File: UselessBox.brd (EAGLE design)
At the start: 49.5 x 39.4 mm, 20 parts, among them Q2 MJE182-VERTICAL, U2 5V, X1 SCREW-TERM-3, X2 SCREW-TERM-3

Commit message: Better power traces and polish tweaks
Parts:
- moved Q2 14.0 mm to (45.7, 50.2)
- moved C6 7.62 mm to (45.1, 38.1)
- moved R2 7.62 mm to (45.7, 45.7)
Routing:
- net N$12: track 23.2 -> 30.8 mm
- net VIN: track 53.1 -> 60.6 mm
- net N$13: track 30.4 -> 25.4 mm
- net N$8: track 24.4 -> 25.1 mm
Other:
- board text added: "SIG"
- board text removed: "CTRL"

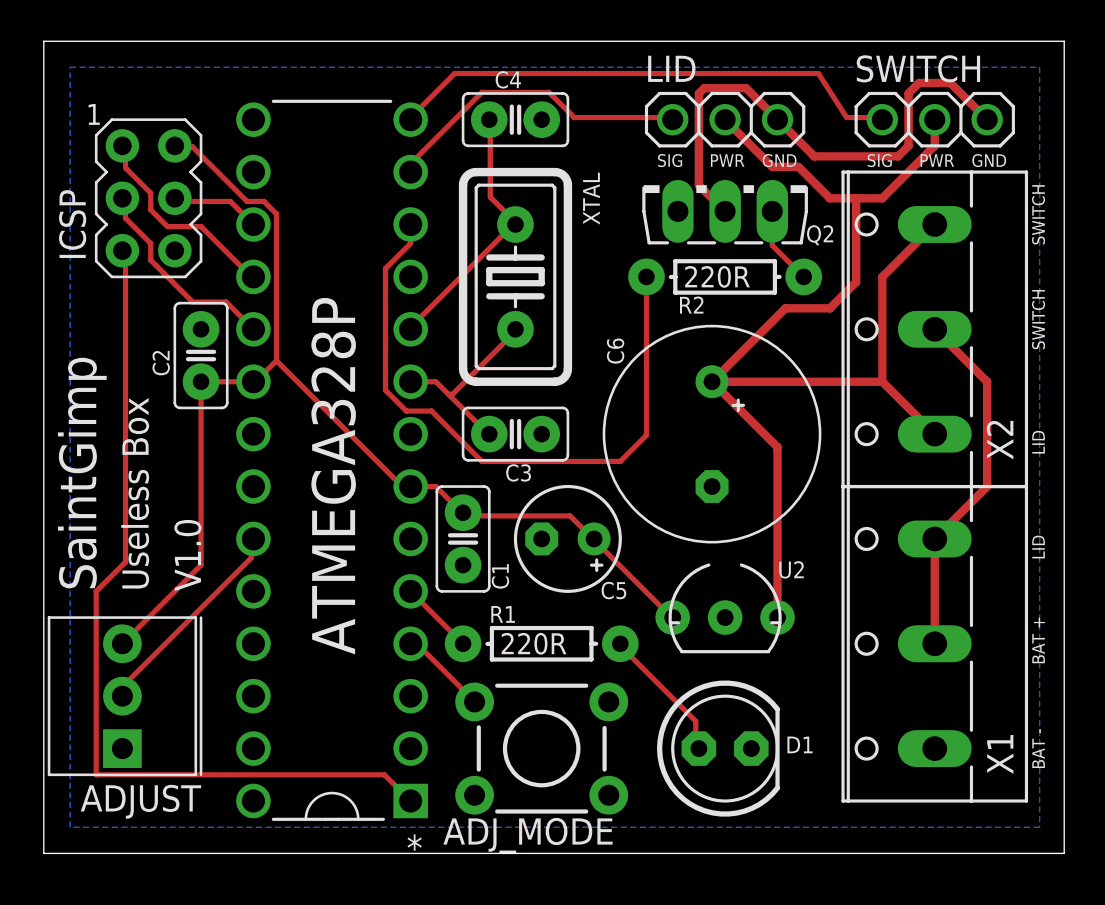
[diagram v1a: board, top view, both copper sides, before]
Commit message: Update size of bypass caps
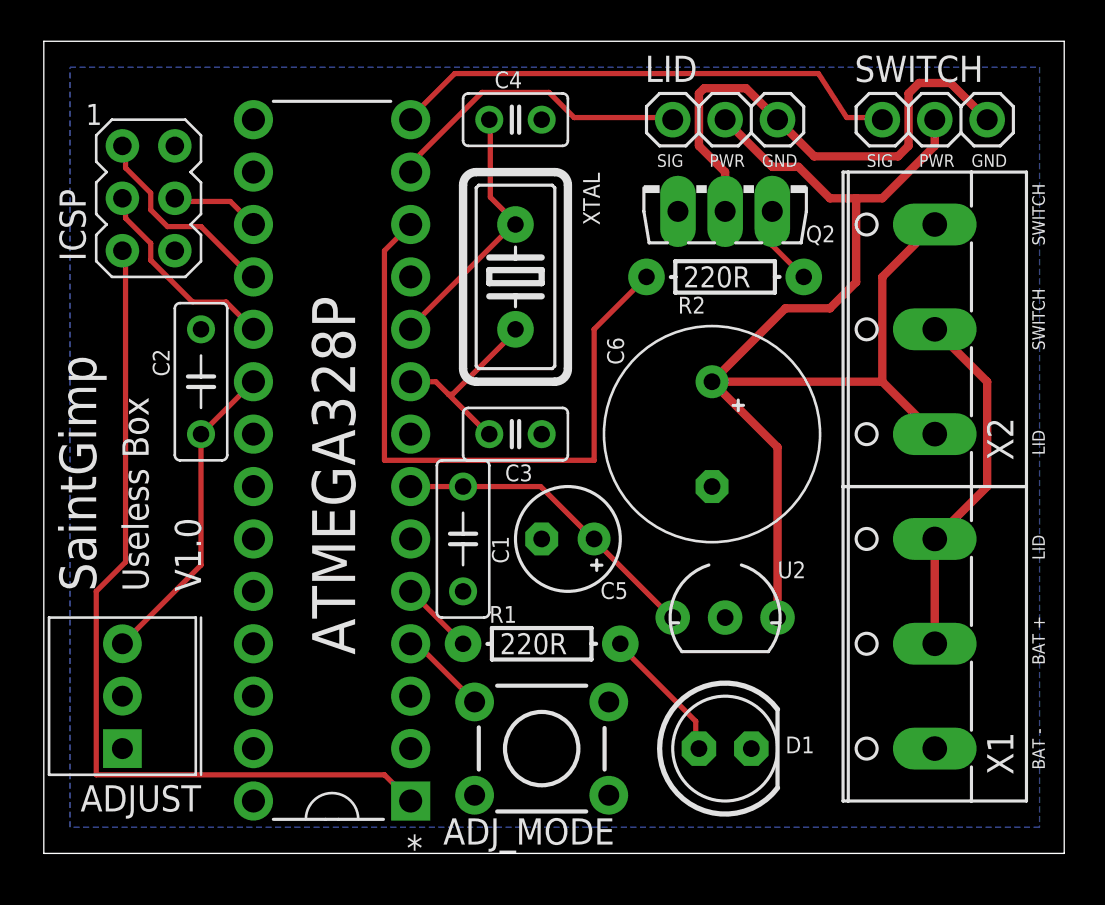
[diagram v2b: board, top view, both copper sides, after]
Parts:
- C1, C2: device SaintGimp:CAPACITOR-2.5MM -> SaintGimp:CAPACITOR-5MM
- moved C1 1.27 mm to (33.0, 33.0)
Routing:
- net VCC: track 56.1 -> 30.7 mm
- net N$15: track 10.3 -> 0.76 mm
- net N$12: track 30.8 -> 32.1 mm
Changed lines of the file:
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@@
 <layer number="97" name="Info" color="7" fill="1" visible="no" active="no"/>
 <layer number="98" name="Guide" color="6" fill="1" visible="no" active="no"/>
+<layer number="99" name="SpiceOrder" color="7" fill="1" visible="no" active="no"/>
 <layer number="100" name="Muster" color="7" fill="1" visible="no" active="no"/>
 <layer number="101" name="Patch_Top" color="12" fill="4" visible="yes" active="yes"/>
@@
 <layer number="111" name="LPC17xx" color="7" fill="1" visible="yes" active="yes"/>
 <layer number="112" name="tSilk" color="7" fill="1" visible="yes" active="yes"/>
+<layer number="113" name="IDFDebug" color="7" fill="1" visible="yes" active="yes"/>
 <layer number="116" name="Patch_BOT" color="9" fill="4" visible="yes" active="yes"/>
 <layer number="121" name="_tsilk" color="7" fill="1" visible="yes" active="yes"/>
@@
 <layer number="251" name="SMDround" color="7" fill="1" visible="no" active="no"/>
 <layer number="254" name="cooling" color="7" fill="1" visible="yes" active="yes"/>
+<layer number="255" name="routoute" color="7" fill="1" visible="yes" active="yes"/>
 </layers>
 <board>
@@
 <param name="msMicroVia" value="13mil"/>
 <param name="msBlindViaRatio" value="0.5"/>
-<param name="rvPadTop" value="0.25"/>
+<param name="rvPadTop" value="0.35"/>
 <param name="rvPadInner" value="0.25"/>
-<param name="rvPadBottom" value="0.25"/>
+<param name="rvPadBottom" value="0.35"/>
 <param name="rvViaOuter" value="0.25"/>
 <param name="rvViaInner" value="0.25"/>
@@
 <attribute name="VALUE" x="30.1244" y="17.145" size="2.0828" layer="27" ratio="10" rot="SR180"/>
 </element>
-<element name="C1" library="SaintGimp" package="CAPACITOR-2.5MM" value="1uF" x="33.02" y="31.75" smashed="yes" rot="R90">
-<attribute name="NAME" x="35.2374375" y="30.5553125" size="0.8128" layer="25" rot="R90"/>
-<attribute name="VALUE" x="35.56" y="31.242" size="1.016" layer="27" rot="R90"/>
-</element>
-<element name="C2" library="SaintGimp" package="CAPACITOR-2.5MM" value="1uF" x="20.32" y="40.64" smashed="yes" rot="R90">
+<element name="C1" library="SaintGimp" package="CAPACITOR-5MM" value="1uF" x="33.02" y="33.02" smashed="yes" rot="R90">
+<attribute name="NAME" x="35.2374375" y="31.8253125" size="0.8128" layer="25" rot="R90"/>
+<attribute name="VALUE" x="35.56" y="32.512" size="1.016" layer="27" rot="R90"/>
+</element>
+<element name="C2" library="SaintGimp" package="CAPACITOR-5MM" value="1uF" x="20.32" y="40.64" smashed="yes" rot="R90">
 <attribute name="NAME" x="18.796" y="40.894" size="0.8128" layer="25" rot="R90"/>
 <attribute name="VALUE" x="22.86" y="40.132" size="1.016" layer="27" rot="R90"/>
@@
 <contactref element="C5" pad="+"/>
 <contactref element="ADJUST" pad="P$3"/>
-<wire x1="31.6992" y1="35.56" x2="30.48" y2="35.56" width="0.254" layer="1"/>
-<wire x1="32.9184" y1="34.3408" x2="31.6992" y2="35.56" width="0.254" layer="1"/>
-<wire x1="32.9184" y1="34.3408" x2="33.02" y2="34.29" width="0.254" layer="1"/>
 <wire x1="43.0784" y1="29.2608" x2="39.4208" y2="32.9184" width="0.254" layer="1"/>
 <wire x1="39.4208" y1="32.9184" x2="39.37" y2="33.02" width="0.254" layer="1"/>
 <wire x1="43.0784" y1="29.2608" x2="43.18" y2="29.21" width="0.254" layer="1"/>
-<wire x1="38.2016" y1="34.1376" x2="33.1216" y2="34.1376" width="0.254" layer="1"/>
-<wire x1="39.2176" y1="33.1216" x2="38.2016" y2="34.1376" width="0.254" layer="1"/>
-<wire x1="33.1216" y1="34.1376" x2="33.02" y2="34.29" width="0.254" layer="1"/>
 <wire x1="39.2176" y1="33.1216" x2="39.37" y2="33.02" width="0.254" layer="1"/>
-<wire x1="19.9136" y1="52.0192" x2="19.1008" y2="52.0192" width="0.254" layer="1"/>
-<wire x1="22.5552" y1="49.3776" x2="19.9136" y2="52.0192" width="0.254" layer="1"/>
-<wire x1="23.368" y1="49.3776" x2="22.5552" y2="49.3776" width="0.254" layer="1"/>
-<wire x1="23.9776" y1="48.768" x2="23.368" y2="49.3776" width="0.254" layer="1"/>
-<wire x1="23.9776" y1="41.656" x2="23.9776" y2="48.768" width="0.254" layer="1"/>
-<wire x1="22.9616" y1="40.64" x2="23.9776" y2="41.656" width="0.254" layer="1"/>
-<wire x1="19.1008" y1="52.0192" x2="19.05" y2="52.07" width="0.254" layer="1"/>
-<wire x1="22.9616" y1="40.64" x2="22.86" y2="40.64" width="0.254" layer="1"/>
-<wire x1="22.86" y1="40.64" x2="20.32" y2="40.64" width="0.254" layer="1"/>
-<wire x1="30.0736" y1="35.56" x2="30.48" y2="35.56" width="0.254" layer="1"/>
-<wire x1="23.9776" y1="41.656" x2="30.0736" y2="35.56" width="0.254" layer="1"/>
-<wire x1="20.32" y1="40.64" x2="20.32" y2="31.75" width="0.254" layer="1"/>
+<wire x1="22.86" y1="40.64" x2="20.32" y2="38.1" width="0.254" layer="1"/>
+<wire x1="20.32" y1="38.1" x2="20.32" y2="31.75" width="0.254" layer="1"/>
 <wire x1="20.32" y1="31.75" x2="16.51" y2="27.94" width="0.254" layer="1"/>
+<wire x1="30.48" y1="35.56" x2="33.02" y2="35.56" width="0.254" layer="1"/>
+<wire x1="33.02" y1="35.56" x2="36.7792" y2="35.56" width="0.254" layer="1"/>
+<wire x1="36.7792" y1="35.56" x2="39.2176" y2="33.1216" width="0.254" layer="1"/>
+<wire x1="22.86" y1="40.64" x2="19.05" y2="52.07" width="0" layer="19" extent="1-1"/>
+<wire x1="30.48" y1="35.56" x2="22.86" y2="40.64" width="0" layer="19" extent="1-1"/>
 </signal>
 <signal name="N$6">
@@
 <contactref element="ATMEGA328P" pad="12"/>
 <contactref element="R2" pad="P$1"/>
-<wire x1="30.48" y1="47.3456" x2="30.48" y2="48.26" width="0.254" layer="1"/>
-<wire x1="29.2608" y1="46.1264" x2="30.48" y2="47.3456" width="0.254" layer="1"/>
-<wire x1="29.2608" y1="40.2336" x2="29.2608" y2="46.1264" width="0.254" layer="1"/>
-<wire x1="30.2768" y1="39.2176" x2="29.2608" y2="40.2336" width="0.254" layer="1"/>
-<wire x1="31.496" y1="39.2176" x2="30.2768" y2="39.2176" width="0.254" layer="1"/>
-<wire x1="33.9344" y1="36.7792" x2="31.496" y2="39.2176" width="0.254" layer="1"/>
-<wire x1="40.64" y1="36.7792" x2="33.9344" y2="36.7792" width="0.254" layer="1"/>
-<wire x1="40.64" y1="36.7792" x2="41.91" y2="38.0492" width="0.254" layer="1"/>
-<wire x1="41.91" y1="38.0492" x2="41.91" y2="45.72" width="0.254" layer="1"/>
+<wire x1="30.48" y1="48.26" x2="29.21" y2="46.99" width="0.254" layer="1"/>
+<wire x1="29.21" y1="46.99" x2="29.21" y2="36.83" width="0.254" layer="1"/>
+<wire x1="29.21" y1="36.83" x2="39.37" y2="36.83" width="0.254" layer="1"/>
+<wire x1="39.37" y1="36.83" x2="39.37" y2="43.18" width="0.254" layer="1"/>
+<wire x1="39.37" y1="43.18" x2="41.91" y2="45.72" width="0.254" layer="1"/>
 </signal>
 <signal name="N$13">
@@
 <wire x1="46.736" y1="54.864" x2="44.704" y2="54.864" width="0.4064" layer="1"/>
 <wire x1="44.704" y1="54.864" x2="44.45" y2="54.61" width="0.4064" layer="1"/>
-<wire x1="44.45" y1="54.61" x2="44.45" y2="50.165" width="0.4064" layer="1"/>
-<wire x1="44.45" y1="50.165" x2="45.72" y2="48.895" width="0.4064" layer="1"/>
+<wire x1="44.45" y1="54.61" x2="44.45" y2="52.07" width="0.4064" layer="1"/>
+<wire x1="44.45" y1="52.07" x2="45.72" y2="50.8" width="0.4064" layer="1"/>
+<wire x1="45.72" y1="50.8" x2="45.72" y2="48.895" width="0.4064" layer="1"/>
 </signal>
 <signal name="N$14">
@@
 <contactref element="ADJUST" pad="P$2"/>
 <contactref element="ATMEGA328P" pad="23"/>
-<wire x1="22.7584" y1="32.1056" x2="22.7584" y2="32.9184" width="0.254" layer="1"/>
-<wire x1="16.6624" y1="26.0096" x2="22.7584" y2="32.1056" width="0.254" layer="1"/>
 <wire x1="16.6624" y1="25.4" x2="16.6624" y2="26.0096" width="0.254" layer="1"/>
-<wire x1="22.7584" y1="32.9184" x2="22.86" y2="33.02" width="0.254" layer="1"/>
 <wire x1="16.6624" y1="25.4" x2="16.51" y2="25.4" width="0.254" layer="1"/>
+<wire x1="16.6624" y1="26.0096" x2="22.86" y2="33.02" width="0" layer="19" extent="1-1"/>
 </signal>
 <signal name="N$18">

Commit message: Update parts from library
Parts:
- ADJUST: device SaintGimp:3362U -> SaintGimp:POT-3362U
- ADJ_MODE: device SaintGimp:TACTILE-PTH -> SaintGimp:TACTILE-SWITCH-6MM
- ATMEGA328P: device SaintGimp:DIP254P762X457-28 -> SaintGimp:DIP28
- Q2: value MJE182-VERTICAL -> MJE182-V; device SaintGimp:TO126AV -> SaintGimp:TO225AA-V
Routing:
- net VCC: track 30.7 -> 57.6 mm
- net N$15: track 0.76 -> 9.92 mm
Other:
- board text added: "V1.1"
- board text removed: "V1.0"
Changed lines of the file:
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@@
 <text x="15.24" y="30.48" size="1.778" layer="121" rot="R90">SaintGimp</text>
 <text x="17.78" y="30.48" size="1.27" layer="121" rot="R90">Useless Box</text>
-<text x="20.32" y="30.48" size="1.27" layer="121" rot="R90">V1.0</text>
+<text x="20.32" y="30.48" size="1.27" layer="121" rot="R90">V1.1</text>
 <text x="47.498" y="51.054" size="0.6096" layer="121">GND</text>
 <text x="57.658" y="51.054" size="0.6096" layer="121">GND</text>
@@
 </class>
 </classes>
-<designrules name="OSHPark *">
+<designrules name="OSHPark">
 <description language="de">&lt;b&gt;EAGLE Design Rules&lt;/b&gt;
 &lt;p&gt;
@@
 </autorouter>
 <elements>
-<element name="ATMEGA328P" library="SaintGimp" package="DIP254P762X457-28" value="ATMEGA328P-PU" x="22.86" y="53.34" smashed="yes" rot="R180">
+<element name="ATMEGA328P" library="SaintGimp" package="DIP28" value="ATMEGA328P-PU" x="22.86" y="53.34" smashed="yes" rot="R180">
 <attribute name="PACKAGE" value="PDIP-28" x="22.86" y="53.34" size="1.778" layer="27" rot="R180" display="off"/>
 <attribute name="OC_NEWARK" value="15R0268" x="22.86" y="53.34" size="1.778" layer="27" rot="R180" display="off"/>
@@
 <attribute name="VALUE" x="41.402" y="33.147" size="1.27" layer="27" ratio="10" rot="R270"/>
 </element>
-<element name="Q2" library="SaintGimp" package="TO126AV" value="MJE182-VERTICAL" x="45.72" y="50.165" smashed="yes">
+<element name="Q2" library="SaintGimp" package="TO225AA-V" value="MJE182-V" x="45.72" y="50.165" smashed="yes">
 <attribute name="NAME" x="49.6316" y="47.3964" size="0.8128" layer="25" ratio="10"/>
 <attribute name="VALUE" x="41.7322" y="43.8404" size="1.27" layer="27" ratio="10"/>
@@
 <element name="X1" library="SaintGimp" package="SCREW-TERM-3" value="SCREW-TERM-3" x="55.88" y="27.94" rot="R90"/>
 <element name="X2" library="SaintGimp" package="SCREW-TERM-3" value="SCREW-TERM-3" x="55.88" y="43.18" rot="R90"/>
-<element name="ADJUST" library="SaintGimp" package="3362U" value="10K" x="19.05" y="22.86" smashed="yes" rot="R90">
+<element name="ADJUST" library="SaintGimp" package="POT-3362U" value="10K" x="19.05" y="22.86" smashed="yes" rot="R90">
 <attribute name="NAME" x="20.32" y="21.082" size="1.27" layer="25" rot="R180"/>
 <attribute name="VALUE" x="21.78695625" y="22.80940625" size="1.27" layer="27" rot="R90"/>
 </element>
-<element name="ADJ_MODE" library="SaintGimp" package="TACTILE-PTH" value="TAC_SWITCHPTH" x="36.83" y="22.86" smashed="yes">
+<element name="ADJ_MODE" library="SaintGimp" package="TACTILE-SWITCH-6MM" value="TAC_SWITCHPTH" x="36.83" y="22.86" smashed="yes">
 <attribute name="NAME" x="32.055215625" y="18.2079375" size="1.27" layer="25" ratio="10"/>
 </element>
@@
 <wire x1="43.0784" y1="29.2608" x2="43.18" y2="29.21" width="0.254" layer="1"/>
 <wire x1="39.2176" y1="33.1216" x2="39.37" y2="33.02" width="0.254" layer="1"/>
-<wire x1="22.86" y1="40.64" x2="20.32" y2="38.1" width="0.254" layer="1"/>
 <wire x1="20.32" y1="38.1" x2="20.32" y2="31.75" width="0.254" layer="1"/>
 <wire x1="20.32" y1="31.75" x2="16.51" y2="27.94" width="0.254" layer="1"/>
@@
 <wire x1="33.02" y1="35.56" x2="36.7792" y2="35.56" width="0.254" layer="1"/>
 <wire x1="36.7792" y1="35.56" x2="39.2176" y2="33.1216" width="0.254" layer="1"/>
-<wire x1="22.86" y1="40.64" x2="19.05" y2="52.07" width="0" layer="19" extent="1-1"/>
-<wire x1="30.48" y1="35.56" x2="22.86" y2="40.64" width="0" layer="19" extent="1-1"/>
+<wire x1="30.48" y1="35.56" x2="29.21" y2="35.56" width="0.254" layer="1"/>
+<wire x1="29.21" y1="35.56" x2="24.13" y2="40.64" width="0.254" layer="1"/>
+<wire x1="24.13" y1="40.64" x2="22.86" y2="40.64" width="0.254" layer="1"/>
+<wire x1="19.05" y1="52.07" x2="24.638" y2="52.07" width="0.254" layer="1"/>
+<wire x1="24.638" y1="52.07" x2="24.638" y2="41.148" width="0.254" layer="1"/>
+<wire x1="24.638" y1="41.148" x2="24.13" y2="40.64" width="0.254" layer="1"/>
+<wire x1="20.32" y1="38.1" x2="22.86" y2="40.64" width="0.254" layer="1"/>
 </signal>
 <signal name="N$6">
@@
 <wire x1="49.276" y1="51.054" x2="48.006" y2="51.054" width="0.4064" layer="1"/>
 <wire x1="48.006" y1="51.054" x2="45.72" y2="53.34" width="0.4064" layer="1"/>
-<wire x1="53.34" y1="40.64" x2="53.34" y2="45.72" width="0.4064" layer="1"/>
-<wire x1="53.34" y1="45.72" x2="55.88" y2="48.26" width="0.4064" layer="1"/>
+<wire x1="53.086" y1="45.466" x2="55.88" y2="48.26" width="0.4064" layer="1"/>
 <wire x1="45.085" y1="40.64" x2="48.641" y2="44.196" width="0.4064" layer="1"/>
 <wire x1="48.641" y1="44.196" x2="50.8" y2="44.196" width="0.4064" layer="1"/>
@@
 <wire x1="52.07" y1="45.466" x2="52.07" y2="49.53" width="0.4064" layer="1"/>
 <wire x1="55.88" y1="38.1" x2="53.34" y2="40.64" width="0.4064" layer="1"/>
-<wire x1="53.34" y1="40.64" x2="45.085" y2="40.64" width="0.4064" layer="1"/>
+<wire x1="53.34" y1="40.64" x2="53.086" y2="40.64" width="0.4064" layer="1"/>
+<wire x1="53.086" y1="40.64" x2="45.085" y2="40.64" width="0.4064" layer="1"/>
 <wire x1="48.26" y1="29.21" x2="48.26" y2="37.465" width="0.4064" layer="1"/>
 <wire x1="48.26" y1="37.465" x2="45.085" y2="40.64" width="0.4064" layer="1"/>
+<wire x1="53.086" y1="45.466" x2="53.086" y2="40.64" width="0.4064" layer="1"/>
 </signal>
 <signal name="N$12">
@@
 <wire x1="55.88" y1="27.94" x2="55.88" y2="33.02" width="0.4064" layer="1"/>
 <wire x1="55.88" y1="33.02" x2="58.42" y2="35.56" width="0.4064" layer="1"/>
-<wire x1="58.42" y1="35.56" x2="58.42" y2="40.64" width="0.4064" layer="1"/>
-<wire x1="58.42" y1="40.64" x2="55.88" y2="43.18" width="0.4064" layer="1"/>
+<wire x1="58.674" y1="40.386" x2="55.88" y2="43.18" width="0.4064" layer="1"/>
+<wire x1="58.674" y1="40.386" x2="58.674" y2="36.068" width="0.4064" layer="1"/>
+<wire x1="58.674" y1="36.068" x2="58.42" y2="35.56" width="0.4064" layer="1"/>
 </signal>
 <signal name="N$15">
 <contactref element="ADJUST" pad="P$2"/>
 <contactref element="ATMEGA328P" pad="23"/>
-<wire x1="16.6624" y1="25.4" x2="16.6624" y2="26.0096" width="0.254" layer="1"/>
-<wire x1="16.6624" y1="25.4" x2="16.51" y2="25.4" width="0.254" layer="1"/>
-<wire x1="16.6624" y1="26.0096" x2="22.86" y2="33.02" width="0" layer="19" extent="1-1"/>
+<wire x1="16.51" y1="25.4" x2="22.86" y2="33.02" width="0.254" layer="1"/>
 </signal>
 <signal name="N$18">
